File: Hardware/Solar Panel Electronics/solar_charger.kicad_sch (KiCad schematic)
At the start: 35 parts, among them J1 Screw_Terminal_SolarPanel_Inp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, U3 LT3652EDD, U4 LTC4411ES5TRMPBF

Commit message: Assigned Footprints (preliminary - just to do a quick layout)
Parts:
- J12: renamed from J?; value NTC Connector -> (none)
- U4: footprint Linear_Technology-LTC4411ES5TRMPBF-* -> (none)
- gave numbers to parts that had none: 14
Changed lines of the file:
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@@
   (symbol (lib_id "power:GND") (at 52.07 128.27 0) (unit 1)
     (in_bom yes) (on_board yes) (fields_autoplaced)
-    (property "Reference" "#PWR?" (id 0) (at 52.07 134.62 0)
+    (property "Reference" "#PWR05" (id 0) (at 52.07 134.62 0)
       (effects (font (size 1.27 1.27)) hide)
     )
@@
   (symbol (lib_id "Connector:Screw_Terminal_01x02") (at 48.26 43.18 180) (unit 1)
     (in_bom yes) (on_board yes)
-    (property "Reference" "J?" (id 0) (at 50.3428 34.925 0))
+    (property "Reference" "J2" (id 0) (at 50.3428 34.925 0))
     (property "Value" "Screw_Terminal_SolarPanel_Input" (id 1) (at 50.3428 37.2364 0))
     (property "Footprint" "" (id 2) (at 48.26 43.18 0)
@@
   (symbol (lib_id "power:GND") (at 111.76 26.67 0) (unit 1)
     (in_bom yes) (on_board yes)
-    (property "Reference" "#PWR?" (id 0) (at 111.76 33.02 0)
+    (property "Reference" "#PWR08" (id 0) (at 111.76 33.02 0)
       (effects (font (size 1.27 1.27)) hide)
     )
@@
   (symbol (lib_id "Device:R_Small") (at 52.07 111.76 0) (unit 1)
     (in_bom yes) (on_board yes) (fields_autoplaced)
-    (property "Reference" "R?" (id 0) (at 54.61 110.4899 0)
+    (property "Reference" "R33" (id 0) (at 54.61 110.4899 0)
       (effects (font (size 1.27 1.27)) (justify left))
     )
@@
   (symbol (lib_id "power:GND") (at 57.15 62.23 0) (unit 1)
     (in_bom yes) (on_board yes)
-    (property "Reference" "#PWR?" (id 0) (at 57.15 68.58 0)
+    (property "Reference" "#PWR07" (id 0) (at 57.15 68.58 0)
       (effects (font (size 1.27 1.27)) hide)
     )
@@
   (symbol (lib_id "power:GND") (at 113.03 64.77 0) (unit 1)
     (in_bom yes) (on_board yes)
-    (property "Reference" "#PWR?" (id 0) (at 113.03 71.12 0)
+    (property "Reference" "#PWR010" (id 0) (at 113.03 71.12 0)
       (effects (font (size 1.27 1.27)) hide)
     )
@@
   (symbol (lib_id "Connector:Screw_Terminal_01x02") (at 48.26 59.69 180) (unit 1)
     (in_bom yes) (on_board yes)
-    (property "Reference" "J?" (id 0) (at 50.3428 51.435 0))
+    (property "Reference" "J8" (id 0) (at 50.3428 51.435 0))
     (property "Value" "Screw_Terminal_SolarPanel_Input" (id 1) (at 50.3428 53.7464 0))
     (property "Footprint" "" (id 2) (at 48.26 59.69 0)
@@
   (symbol (lib_id "Connector:Screw_Terminal_01x02") (at 102.87 24.13 180) (unit 1)
     (in_bom yes) (on_board yes)
-    (property "Reference" "J?" (id 0) (at 104.9528 15.875 0))
+    (property "Reference" "J9" (id 0) (at 104.9528 15.875 0))
     (property "Value" "Screw_Terminal_SolarPanel_Input" (id 1) (at 104.9528 18.1864 0))
     (property "Footprint" "" (id 2) (at 102.87 24.13 0)
@@
   (symbol (lib_id "Device:R_Small") (at 40.64 111.76 0) (unit 1)
     (in_bom yes) (on_board yes) (fields_autoplaced)
-    (property "Reference" "R?" (id 0) (at 43.18 110.4899 0)
+    (property "Reference" "R30" (id 0) (at 43.18 110.4899 0)
       (effects (font (size 1.27 1.27)) (justify left))
     )
@@
   (symbol (lib_id "power:GND") (at 57.15 45.72 0) (unit 1)
     (in_bom yes) (on_board yes)
-    (property "Reference" "#PWR?" (id 0) (at 57.15 52.07 0)
+    (property "Reference" "#PWR06" (id 0) (at 57.15 52.07 0)
       (effects (font (size 1.27 1.27)) hide)
     )
@@
   (symbol (lib_id "Device:R_Small") (at 46.99 95.25 90) (unit 1)
     (in_bom yes) (on_board yes)
-    (property "Reference" "R?" (id 0) (at 45.8216 93.7514 0)
+    (property "Reference" "R32" (id 0) (at 45.8216 93.7514 0)
       (effects (font (size 1.27 1.27)) (justify left))
     )
@@
   (symbol (lib_id "Connector:Conn_01x02_Male") (at 114.3 146.05 0) (unit 1)
     (in_bom yes) (on_board yes) (fields_autoplaced)
-    (property "Reference" "J?" (id 0) (at 114.935 140.97 0))
-    (property "Value" "NTC Connector" (id 1) (at 114.935 143.51 0))
+    (property "Reference" "J12" (id 0) (at 114.935 140.97 0))
+    (property "Value" "" (id 1) (at 114.935 143.51 0))
     (property "Footprint" "" (id 2) (at 114.3 146.05 0)
       (effects (font (size 1.27 1.27)) hide)
@@
   (symbol (lib_id "Connector:Screw_Terminal_01x02") (at 104.14 62.23 180) (unit 1)
     (in_bom yes) (on_board yes)
-    (property "Reference" "J?" (id 0) (at 106.2228 53.975 0))
+    (property "Reference" "J11" (id 0) (at 106.2228 53.975 0))
     (property "Value" "Screw_Terminal_SolarPanel_Input" (id 1) (at 106.2228 56.2864 0))
     (property "Footprint" "" (id 2) (at 104.14 62.23 0)
@@
   (symbol (lib_id "Device:R_Small") (at 52.07 120.65 0) (unit 1)
     (in_bom yes) (on_board yes) (fields_autoplaced)
-    (property "Reference" "R?" (id 0) (at 54.61 119.3799 0)
+    (property "Reference" "R34" (id 0) (at 54.61 119.3799 0)
       (effects (font (size 1.27 1.27)) (justify left))
     )
@@
   (symbol (lib_id "Connector_Generic:Conn_01x02") (at 214.63 132.08 0) (unit 1)
     (in_bom yes) (on_board yes) (fields_autoplaced)
-    (property "Reference" "J?" (id 0) (at 217.17 132.0799 0)
+    (property "Reference" "J13" (id 0) (at 217.17 132.0799 0)
       (effects (font (size 1.27 1.27)) (justify left))
     )
@@
   (symbol (lib_id "Connector:TestPoint") (at 151.13 123.19 180) (unit 1)
     (in_bom yes) (on_board yes) (fields_autoplaced)
-    (property "Reference" "TP?" (id 0) (at 153.67 125.2219 0)
+    (property "Reference" "TP7" (id 0) (at 153.67 125.2219 0)
       (effects (font (size 1.27 1.27)) (justify right))
     )
@@
   (symbol (lib_id "power:GND") (at 113.03 46.99 0) (unit 1)
     (in_bom yes) (on_board yes)
-    (property "Reference" "#PWR?" (id 0) (at 113.03 53.34 0)
+    (property "Reference" "#PWR09" (id 0) (at 113.03 53.34 0)
       (effects (font (size 1.27 1.27)) hide)
     )
@@
   (symbol (lib_id "Connector:TestPoint") (at 213.36 95.25 0) (unit 1)
     (in_bom yes) (on_board yes) (fields_autoplaced)
-    (property "Reference" "TP?" (id 0) (at 215.9 90.6779 0)
+    (property "Reference" "TP8" (id 0) (at 215.9 90.6779 0)
       (effects (font (size 1.27 1.27)) (justify left))
     )
@@
   (symbol (lib_id "power:GND") (at 40.64 128.27 0) (unit 1)
     (in_bom yes) (on_board yes) (fields_autoplaced)
-    (property "Reference" "#PWR?" (id 0) (at 40.64 134.62 0)
+    (property "Reference" "#PWR04" (id 0) (at 40.64 134.62 0)
       (effects (font (size 1.27 1.27)) hide)
     )
@@
   (symbol (lib_id "Connector:TestPoint") (at 69.85 95.25 0) (unit 1)
     (in_bom yes) (on_board yes) (fields_autoplaced)
-    (property "Reference" "TP?" (id 0) (at 72.39 90.6779 0)
+    (property "Reference" "TP6" (id 0) (at 72.39 90.6779 0)
       (effects (font (size 1.27 1.27)) (justify left))
     )
@@
   (symbol (lib_id "Connector:Screw_Terminal_01x02") (at 104.14 44.45 180) (unit 1)
     (in_bom yes) (on_board yes)
-    (property "Reference" "J?" (id 0) (at 106.2228 36.195 0))
+    (property "Reference" "J10" (id 0) (at 106.2228 36.195 0))
     (property "Value" "Screw_Terminal_SolarPanel_Input" (id 1) (at 106.2228 38.5064 0))
     (property "Footprint" "" (id 2) (at 104.14 44.45 0)
@@
     (property "Reference" "U4" (id 0) (at 177.8 113.03 0))
     (property "Value" "LTC4411ES5TRMPBF" (id 1) (at 177.8 115.57 0))
-    (property "Footprint" "Linear_Technology-LTC4411ES5TRMPBF-*" (id 2) (at 165.1 110.49 0)
+    (property "Footprint" "" (id 2) (at 165.1 110.49 0)
       (effects (font (size 1.27 1.27)) (justify left) hide)
     )
@@
   (symbol (lib_id "Device:R_Small") (at 40.64 120.65 0) (unit 1)
     (in_bom yes) (on_board yes) (fields_autoplaced)
-    (property "Reference" "R?" (id 0) (at 43.18 119.3799 0)
-      (effects (font (size 1.27 1.27)) (justify left))
-    )
+    (property "Reference" "R31" (id 0) (at 43.18 119.3799 0)
+      (effects (font (size 1.27 1.27)) (justify left))
+    )

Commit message: Add Antenna
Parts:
- C3, C4, C5: footprint (none) -> Capacitor_SMD:C_0603_1608Metric
- D10, D2, D6, D9: footprint (none) -> Diode_SMD:D_SOD-128
- D7, D8: footprint (none) -> LED_SMD:LED_0603_1608Metric
- J1, J10, J11, J2, J8, J9: footprint (none) -> TerminalBlock_TE-Connectivity:TerminalBlock_TE_282834-2_1x02_P2.54mm_Horizontal
- J12: value (none) -> NTC Connector; footprint (none) -> Connector_PinHeader_2.54mm:PinHeader_1x02_P2.54mm_Vertical
- L1: footprint (none) -> Inductor_SMD:L_0603_1608Metric
- R10, R11, R13, R14, R15, R30, R31, R32, R33, R34, R8, R9: footprint (none) -> Resistor_SMD:R_0603_1608Metric
- TP6, TP7, TP8: footprint (none) -> TestPoint:TestPoint_Pad_D1.0mm
- U4: footprint (none) -> LTC4411:Linear_Technology-LTC4411ES5TRMPBF-Level_A

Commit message: Layed out parts a bit more
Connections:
- net at R11.1: now also D8.1 (K)
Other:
- moved on the sheet: R11
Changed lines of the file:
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@@
   (junction (at 209.55 95.25) (diameter 0) (color 0 0 0 0)
   )
+  (junction (at 83.82 95.25) (diameter 0) (color 0 0 0 0)
+  )
   (junction (at 40.64 115.57) (diameter 0) (color 0 0 0 0)
   )
@@
   (junction (at 69.85 95.25) (diameter 0) (color 0 0 0 0)
   )
-  (junction (at 83.82 95.25) (diameter 0) (color 0 0 0 0)
-  )
   (junction (at 187.96 153.67) (diameter 0) (color 0 0 0 0)
   )
@@
     (stroke (width 0) (type default) (color 0 0 0 0))
   )
-  (wire (pts (xy 83.82 107.95) (xy 83.82 123.19))
+  (wire (pts (xy 83.82 110.49) (xy 83.82 123.19))
     (stroke (width 0) (type default) (color 0 0 0 0))
   )
@@
     (stroke (width 0) (type default) (color 0 0 0 0))
   )
+  (wire (pts (xy 83.82 95.25) (xy 83.82 96.52))
+    (stroke (width 0) (type default) (color 0 0 0 0))
+  )
   (wire (pts (xy 138.43 123.19) (xy 138.43 118.11))
     (stroke (width 0) (type default) (color 0 0 0 0))
@@
     (stroke (width 0) (type default) (color 0 0 0 0))
   )
-  (wire (pts (xy 83.82 95.25) (xy 83.82 96.52))
-    (stroke (width 0) (type default) (color 0 0 0 0))
-  )
   (wire (pts (xy 209.55 134.62) (xy 201.93 134.62))
     (stroke (width 0) (type default) (color 0 0 0 0))
@@
     (stroke (width 0) (type default) (color 0 0 0 0))
   )
+  (wire (pts (xy 83.82 95.25) (xy 90.17 95.25))
+    (stroke (width 0) (type default) (color 0 0 0 0))
+  )
   (wire (pts (xy 146.05 118.11) (xy 146.05 120.65))
     (stroke (width 0) (type default) (color 0 0 0 0))
@@
     (stroke (width 0) (type default) (color 0 0 0 0))
   )
-  (wire (pts (xy 83.82 95.25) (xy 90.17 95.25))
-    (stroke (width 0) (type default) (color 0 0 0 0))
-  )
   (wire (pts (xy 162.56 120.65) (xy 162.56 123.19))
     (stroke (width 0) (type default) (color 0 0 0 0))
@@
   )
   (wire (pts (xy 113.03 95.25) (xy 105.41 95.25))
+    (stroke (width 0) (type default) (color 0 0 0 0))
+  )
+  (wire (pts (xy 83.82 104.14) (xy 83.82 105.41))
     (stroke (width 0) (type default) (color 0 0 0 0))
   )
@@
     (pin "2")
   )
-  (symbol (lib_id "Device:R_Small") (at 83.82 105.41 0) (unit 1)
-    (in_bom yes) (on_board yes)
-    (property "Reference" "R11" (id 0) (at 85.3186 104.2416 0)
-      (effects (font (size 1.27 1.27)) (justify left))
-    )
-    (property "Value" "10k" (id 1) (at 85.3186 106.553 0)
-      (effects (font (size 1.27 1.27)) (justify left))
-    )
-    (property "Footprint" "Resistor_SMD:R_0603_1608Metric" (id 2) (at 83.82 105.41 0)
-      (effects (font (size 1.27 1.27)) hide)
-    )
-    (property "Datasheet" "~" (id 3) (at 83.82 105.41 0)
-      (effects (font (size 1.27 1.27)) hide)
-    )
+  (symbol (lib_id "Device:R_Small") (at 83.82 107.95 0) (unit 1)
+    (in_bom yes) (on_board yes)
+    (property "Reference" "R11" (id 0) (at 85.3186 106.7816 0)
+      (effects (font (size 1.27 1.27)) (justify left))
+    )
+    (property "Value" "10k" (id 1) (at 85.3186 109.093 0)
+      (effects (font (size 1.27 1.27)) (justify left))
+    )
+    (property "Footprint" "Resistor_SMD:R_0603_1608Metric" (id 2) (at 83.82 107.95 0)
+      (effects (font (size 1.27 1.27)) hide)
+    )
+    (property "Datasheet" "~" (id 3) (at 83.82 107.95 0)
+      (effects (font (size 1.27 1.27)) hide)
+    )

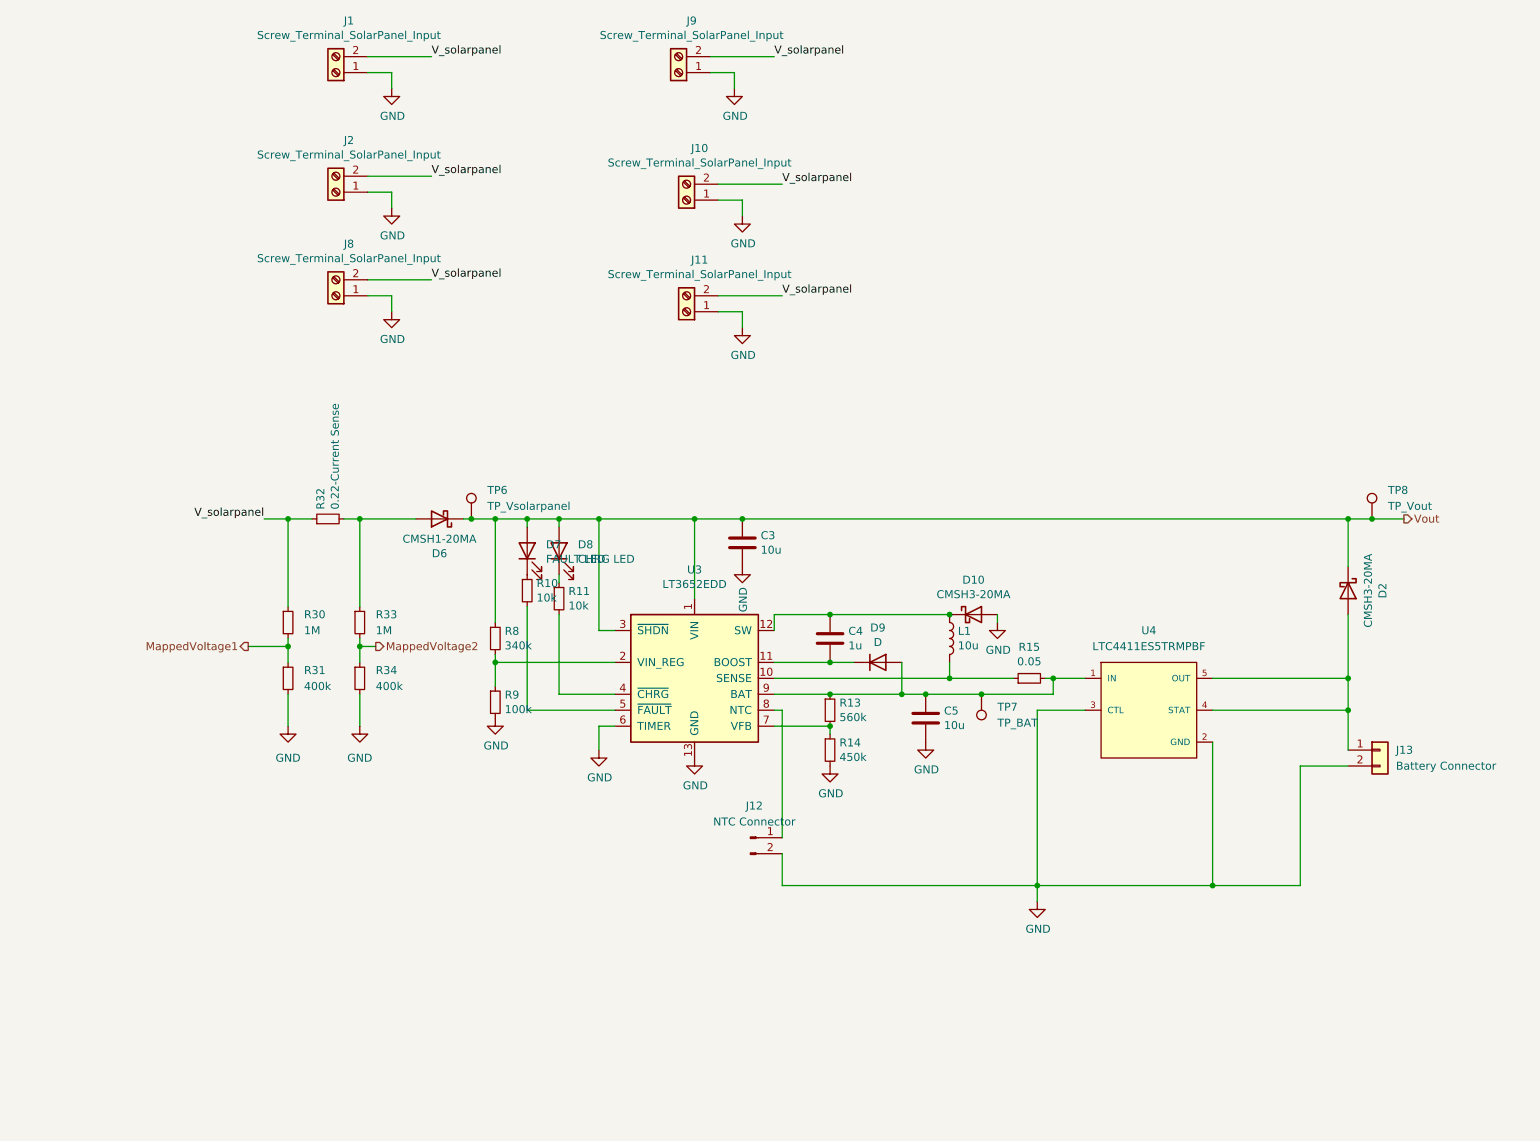
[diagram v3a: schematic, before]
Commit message: Added another ADS component. Layout and routing can be continued.
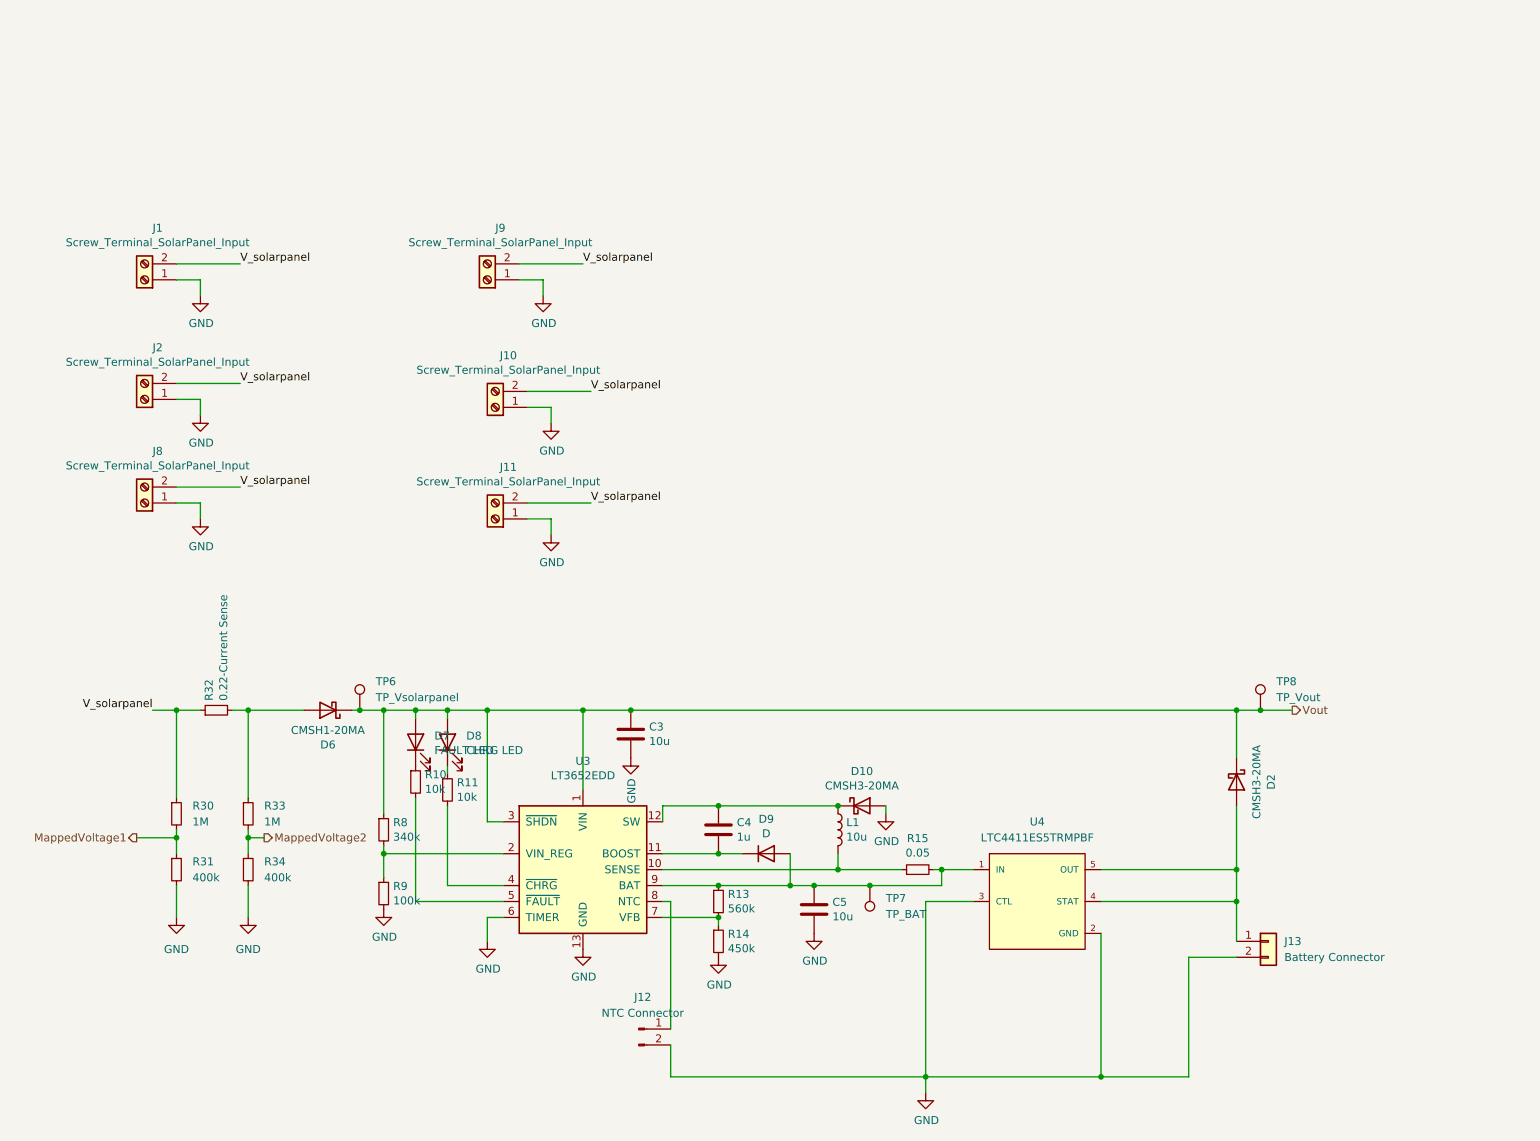
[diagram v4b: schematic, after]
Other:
- moved on the sheet: C3, C4, C5, D10, D2, D6, D7, D8, D9, J1, J10, J11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

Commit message: ICARUS v2
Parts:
- removed J10, J11, J2, J8, J9: Screw_Terminal_SolarPanel_Input, TerminalBlock_TE-Connectivity:TerminalBlock_TE_282834-2_1x02_P2.54mm_Horizontal, symbol Connector:Screw_Terminal_01x02
- removed J12: NTC Connector, Connector_PinHeader_2.54mm:PinHeader_1x02_P2.54mm_Vertical, symbol Connector:Conn_01x02_Male
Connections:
- net GND: no longer J1.1 (Pin_1)
- new net GNDA: J1.1 (Pin_1)
